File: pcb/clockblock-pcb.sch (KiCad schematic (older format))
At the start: 77 parts, among them IC1 TLC5971, IC2 TLC5971, IC3 TLC5971, IC4 PCF2129AT, IC5 TLV71333, IC6 ATTINY87/167_SO, IC7 FT230X_SOP, J1 ARM, J2 MICROUSB, P1 ARM0, P10 ARM9, P11 ARM10, P12 ARM11, P13 USBtoMAIN, P14 AVR_ISP, P15 MAINtoUSB, P2 ARM1, P3 ARM2, P4 ARM3, P5 ARM4, P6 ARM5, P7 ARM6, P8 ARM7, P9 ARM8

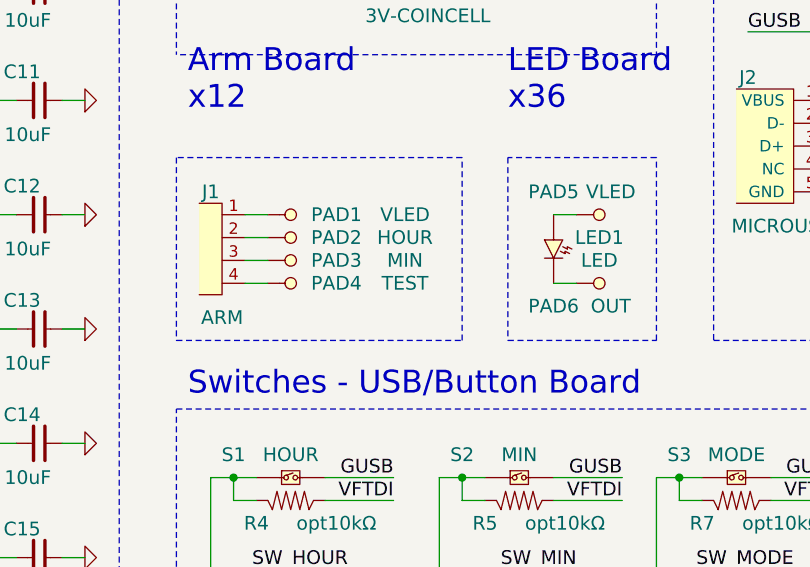
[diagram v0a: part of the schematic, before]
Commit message: got started on the layout and footprint selection
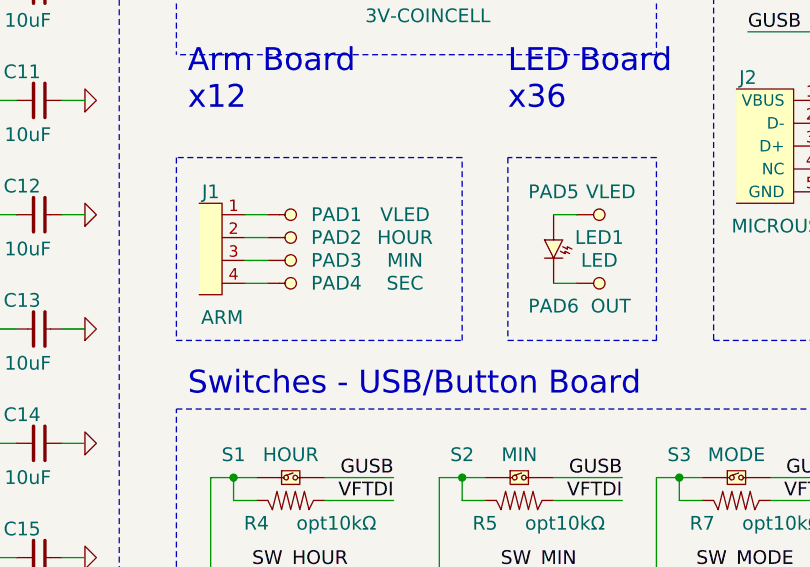
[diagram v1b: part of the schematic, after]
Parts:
- PAD4: value TEST -> SEC
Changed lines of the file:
@@
 P 4500 5400
 F 0 "PAD4" H 4300 5400 60  0000 C CNN
-F 1 "TEST" H 4000 5400 60  0000 C CNN
+F 1 "SEC" H 4000 5400 60  0000 C CNN
 F 2 "~" H 4500 5400 60  0001 C CNN
 F 3 "~" H 4500 5400 60  0001 C CNN
@@
 E1 7A 30 2F E3 9E BF BB FC D0 5C 2F 77 12 1D A4 F0 58 02 39 97 10 5D 3F 53 4D 5C E7 C1 2F 96 BB
 0B B8 4B 44 66 C0 DD 9B E5 70 E1 99 33 E3 22 76 A6 C0 F5 70 86 E1 7A 3C 1F 00 F7 E2 62 F9 87 B5
-4B 6B 3B F8 7F 51 4C 22 23 01 FF ED 6E 00 00 00 00 49 45 4E 44 AE 42 60 82 0A $EndBitmap
+4B 6B 3B F8 7F 51 4C 22 23 01 FF ED 6E 00 00 00 00 49 45 4E 44 AE 42 60 82 34 $EndBitmap
 EndData
 $EndBitmap
@@
 00 00 80 1C 90 88 03 00 00 00 00 00 00 72 40 22 0E 00 00 00 00 00 00 C8 01 89 38 00 00 00 00 00
 00 20 07 24 E2 00 00 00 00 00 00 80 1C FC FF 3E 6A 41 A6 FA 5D A5 94 00 00 00 00 49 45 4E 44 AE
-42 60 82 8D $EndBitmap
+42 60 82 97 $EndBitmap
 EndData
 $EndBitmap

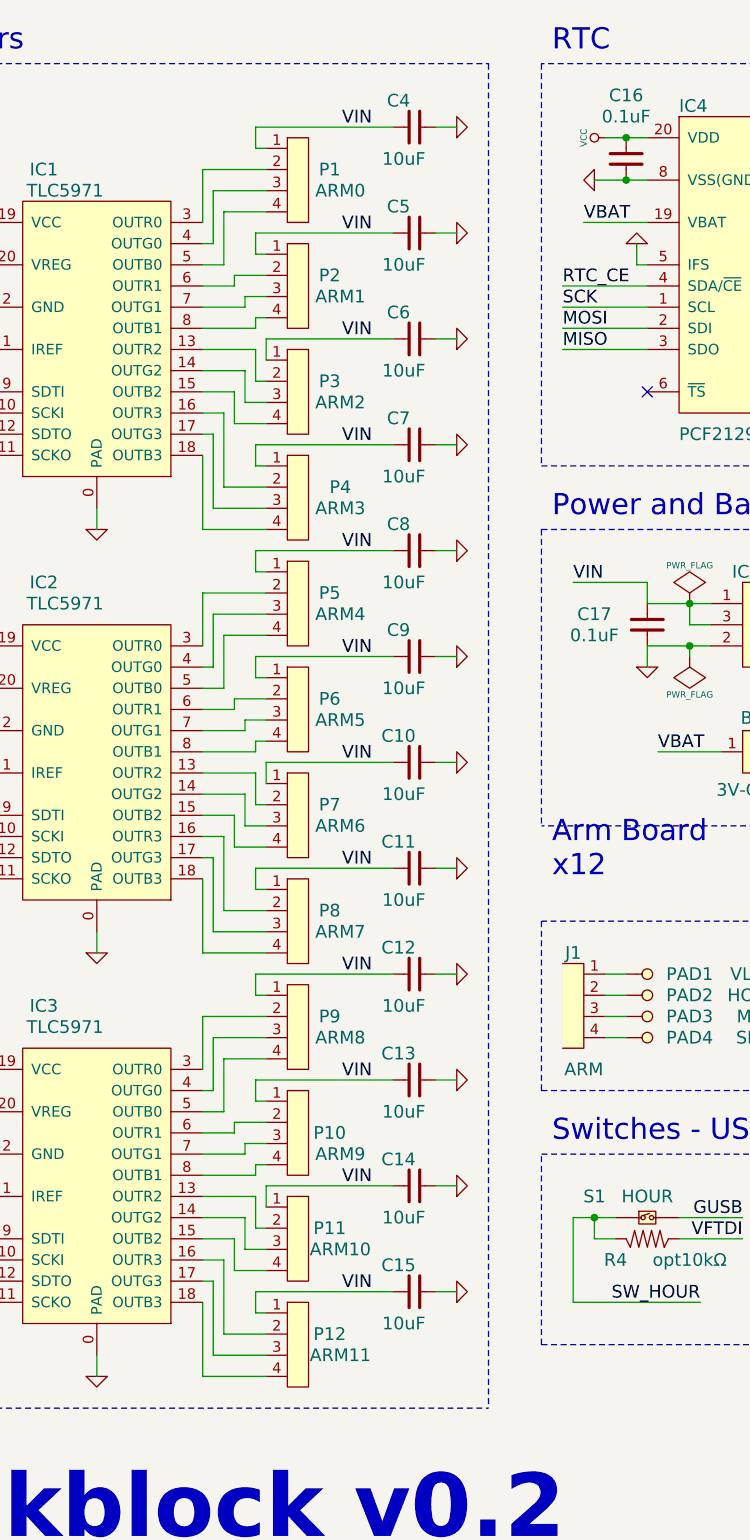
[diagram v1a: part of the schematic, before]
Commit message: trying out spring connections for arms
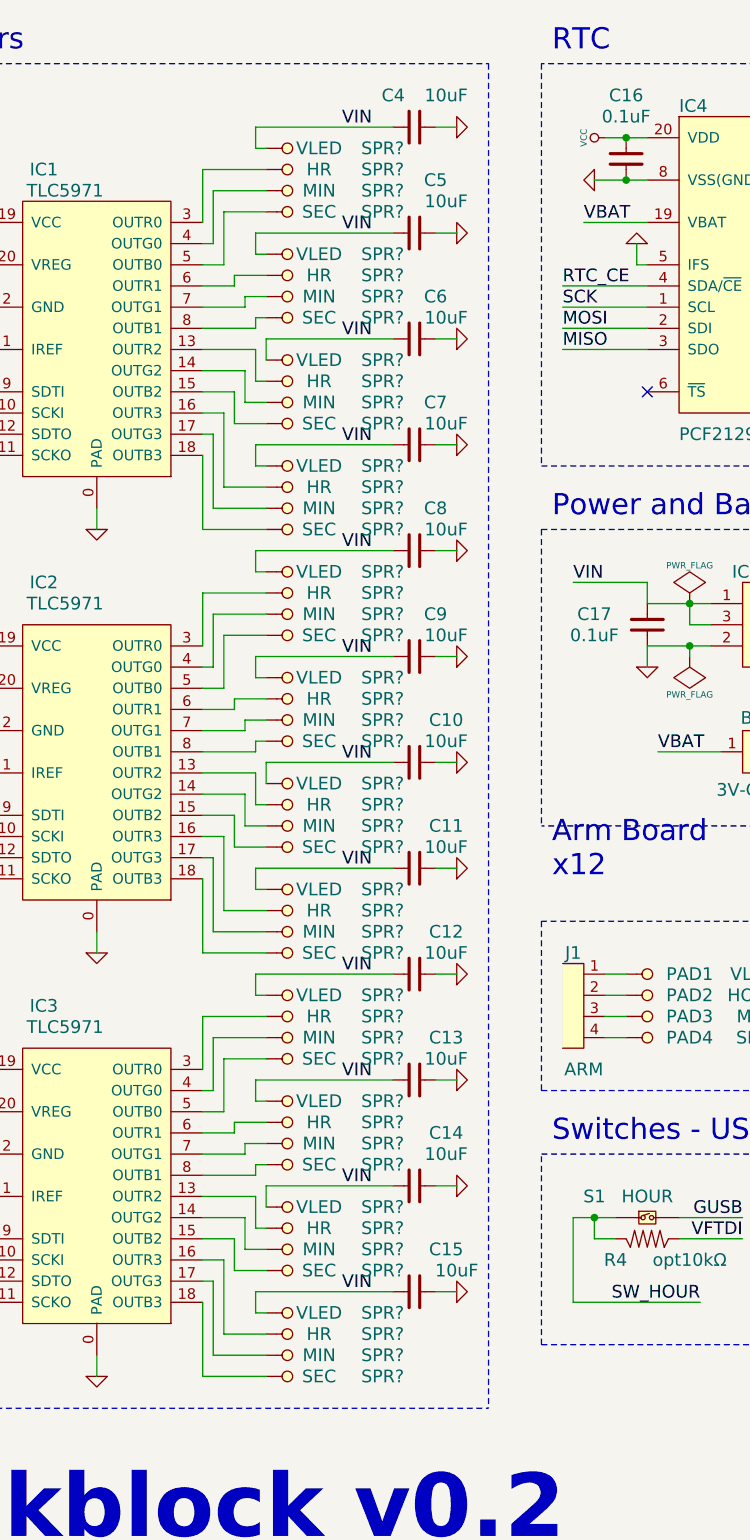
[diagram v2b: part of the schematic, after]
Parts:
- removed P1: ARM0, ~, symbol 4PIN_HEADER
- removed P10: ARM9, ~, symbol 4PIN_HEADER
- removed P11: ARM10, ~, symbol 4PIN_HEADER
- removed P12: ARM11, ~, symbol 4PIN_HEADER
- removed P2: ARM1, ~, symbol 4PIN_HEADER
- removed P3: ARM2, ~, symbol 4PIN_HEADER
- removed P4: ARM3, ~, symbol 4PIN_HEADER
- removed P5: ARM4, ~, symbol 4PIN_HEADER
- removed P6: ARM5, ~, symbol 4PIN_HEADER
- removed P7: ARM6, ~, symbol 4PIN_HEADER
- removed P8: ARM7, ~, symbol 4PIN_HEADER
- removed P9: ARM8, ~, symbol 4PIN_HEADER
- added SPR? (x12): VLED, ~, symbol TEST
- added SPR? (x12): HR, ~, symbol TEST
- added SPR? (x12): MIN, ~, symbol TEST
- added SPR? (x12): SEC, ~, symbol TEST
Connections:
- net VIN: now also SPR?.1 (TP), SPR?.1 (TP), SPR?.1 (TP), SPR?.1 (TP), SPR?.1 (TP), SPR?.1 (TP), SPR?.1 (TP), SPR?.1 (TP), SPR?.1 (TP), SPR?.1 (TP), SPR?.1 (TP), SPR?.1 (TP)
- net at IC3.13 (OUTR2): now also SPR?.1 (TP)
- net at IC3.14 (OUTG2): now also SPR?.1 (TP)
- net at IC3.15 (OUTB2): now also SPR?.1 (TP)
- net at IC3.16 (OUTR3): now also SPR?.1 (TP)
- net at IC3.17 (OUTG3): now also SPR?.1 (TP)
- net at IC3.18 (OUTB3): now also SPR?.1 (TP)
- net at IC3.3 (OUTR0): now also SPR?.1 (TP)
- net at IC3.4 (OUTG0): now also SPR?.1 (TP)
- net at IC3.5 (OUTB0): now also SPR?.1 (TP)
- net at IC3.6 (OUTR1): now also SPR?.1 (TP)
- net at IC3.7 (OUTG1): now also SPR?.1 (TP)
- net at IC3.8 (OUTB1): now also SPR?.1 (TP)
- net at IC2.13 (OUTR2): now also SPR?.1 (TP)
- net at IC2.14 (OUTG2): now also SPR?.1 (TP)
- net at IC2.15 (OUTB2): now also SPR?.1 (TP)
- net at IC2.16 (OUTR3): now also SPR?.1 (TP)
- net at IC2.17 (OUTG3): now also SPR?.1 (TP)
- net at IC2.18 (OUTB3): now also SPR?.1 (TP)
- net at IC2.3 (OUTR0): now also SPR?.1 (TP)
- net at IC2.4 (OUTG0): now also SPR?.1 (TP)
- net at IC2.5 (OUTB0): now also SPR?.1 (TP)
- net at IC2.6 (OUTR1): now also SPR?.1 (TP)
- net at IC2.7 (OUTG1): now also SPR?.1 (TP)
- net at IC2.8 (OUTB1): now also SPR?.1 (TP)
- net at IC1.13 (OUTR2): now also SPR?.1 (TP)
- net at IC1.14 (OUTG2): now also SPR?.1 (TP)
- net at IC1.15 (OUTB2): now also SPR?.1 (TP)
- net at IC1.16 (OUTR3): now also SPR?.1 (TP)
- net at IC1.17 (OUTG3): now also SPR?.1 (TP)
- net at IC1.18 (OUTB3): now also SPR?.1 (TP)
- net at IC1.3 (OUTR0): now also SPR?.1 (TP)
- net at IC1.4 (OUTG0): now also SPR?.1 (TP)
- net at IC1.5 (OUTB0): now also SPR?.1 (TP)
- net at IC1.6 (OUTR1): now also SPR?.1 (TP)
- net at IC1.7 (OUTG1): now also SPR?.1 (TP)
- net at IC1.8 (OUTB1): now also SPR?.1 (TP)

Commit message: initial footprint selection done
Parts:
- removed J1: ARM, ~, symbol 4PIN_FEMALE
- added LND?: VLED, ~, symbol TEST
- added LND?: HOUR, ~, symbol TEST
- added LND?: MIN, ~, symbol TEST
- added LND?: SEC, ~, symbol TEST
- gave numbers to parts that had none: 48
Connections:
- net at PAD1.1 (TP): now also LND?.1 (TP)
- net at PAD2.1 (TP): now also LND?.1 (TP)
- net at PAD3.1 (TP): now also LND?.1 (TP)
- net at PAD4.1 (TP): now also LND?.1 (TP)
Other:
- moved on the sheet: PAD1, PAD2, PAD3, PAD4

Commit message: continuing work on schematic and layout
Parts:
- BT1: footprint ~ -> LINX_BAT-HLD-012-SMT; Manufacturer (none) -> Linx; Part (none) -> BAT-HLD-012-SMT
- C1, C10, C11, C12, C13, C14, C15, C16, C17, C18, C19, C2, C20, C21, C22, C23, C24, C26, C3, C4, C5, C6, C7, C8, C9, FB1, R1, R10, R11, R12, R2, R3, R4, R5, R6, R7, R8, R9: footprint ~ -> 0603(1608m)
- C25: footprint ~ -> 0805(2012m)_tant-cap; Manufacturer (none) -> Kemet; Part (none) -> T491A475K010AT
- IC1, IC2, IC3: footprint ~ -> HTSSOP20
- IC4: footprint ~ -> SOIC20
- IC5: footprint ~ -> SOT23-5; Manufacturer Texas_Instruments -> TI; Part (none) -> TLV71333PDBV
- IC6: value ATTINY87/167_SO -> ATTINY87/167; footprint (none) -> TSSOP20; Part (none) -> ATTINY167-XU
- IC7: value FT230X_SOP -> FT230X; footprint ~ -> SSOP16; Manufacturer (none) -> FTDI; Part (none) -> FT230XS
- J2: value MICROUSB -> USB; footprint ~ -> MICROUSB_sm; Manufacturer (none) -> FCI; Part (none) -> 10118192-0001LF
- LED1: footprint ~ -> LED-5mm; Manufacturer (none) -> Vishay; Part (none) -> TLCR5800
- LED2, LED3, LED4: footprint ~ -> 0603(1608m)_led
- LND1, LND2, LND3, LND4: renamed from LND?; footprint ~ -> TE_1551573-5_SPRING-FINGER; Manufacturer (none) -> N/A; Part (none) -> N/A
- P13, P15: footprint ~ -> 2x5-array
- P14: footprint ~ -> 2x3-array; Manufacturer (none) -> N/A; Part (none) -> N/A
- PAD1, PAD2, PAD3, PAD4, PAD5, PAD6: footprint ~ -> 3x5MM_SM-PAD; Manufacturer (none) -> N/A; Part (none) -> N/A
- S1, S2, S3: footprint ~ -> SPST_6MM_sm; Manufacturer (none) -> TE Connectivity; Part (none) -> FSM4JSMA
- SPR1, SPR10, SPR11, SPR12, SPR13, SPR14, SPR15, SPR16, SPR17, SPR18, SPR19, SPR2, SPR20, SPR21, SPR22, SPR23, SPR24, SPR25, SPR26, SPR27, SPR28, SPR29, SPR3, SPR30, SPR31, SPR32, SPR33, SPR34, SPR35, SPR36, SPR37, SPR38, SPR39, SPR4, SPR40, SPR41, SPR42, SPR43, SPR44, SPR45, SPR46, SPR47, SPR48, SPR5, SPR6, SPR7, SPR8, SPR9: footprint ~ -> TE_1551573-5_SPRING-FINGER
